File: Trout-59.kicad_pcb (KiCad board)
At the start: 2 copper layers, 304.8 x 77.8 mm, 138 parts, among them SW1 SW_Push, U1 ATmega32U4-AU, U2 SRV05-4, Y1 16MHz

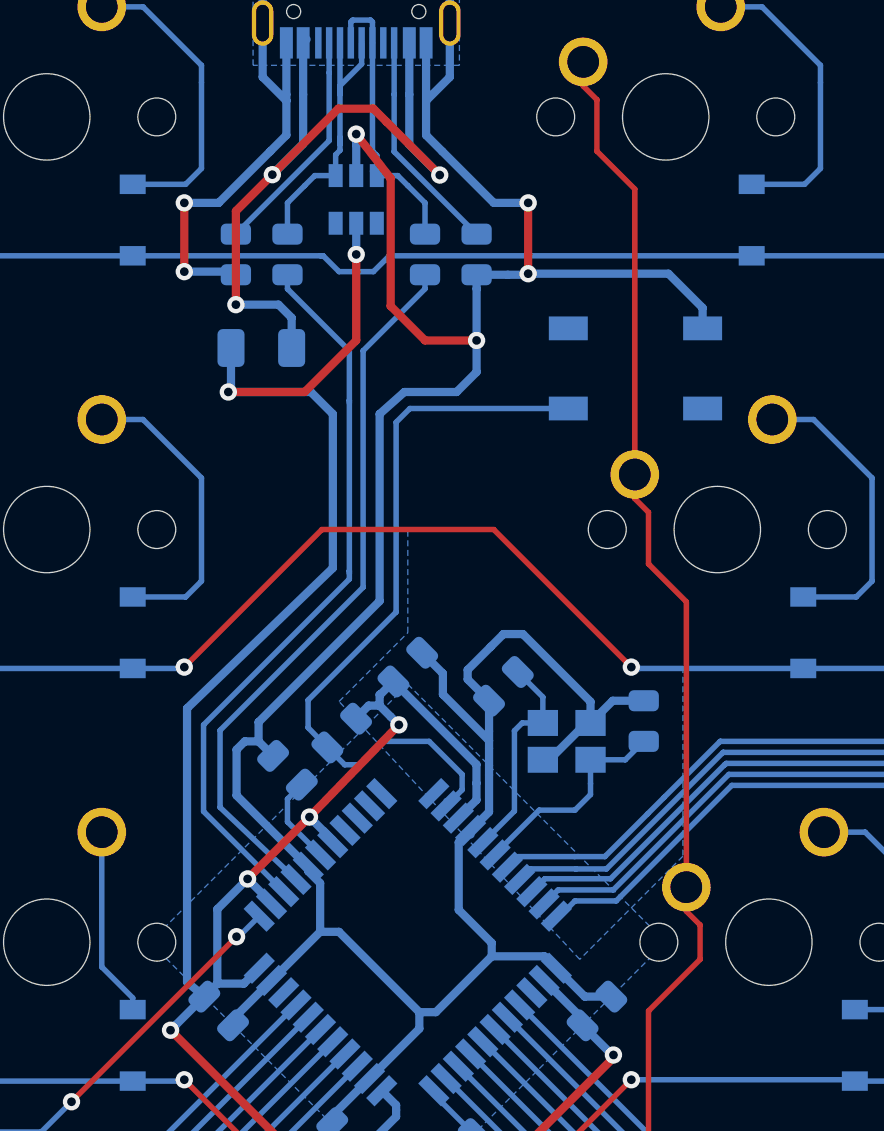
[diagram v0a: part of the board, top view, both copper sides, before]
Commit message: Multiple changes to USB/crystal routingv
Crystal ground plane defined, C2 and crystal location updated, row 0 rerouted, and Fuse rotated
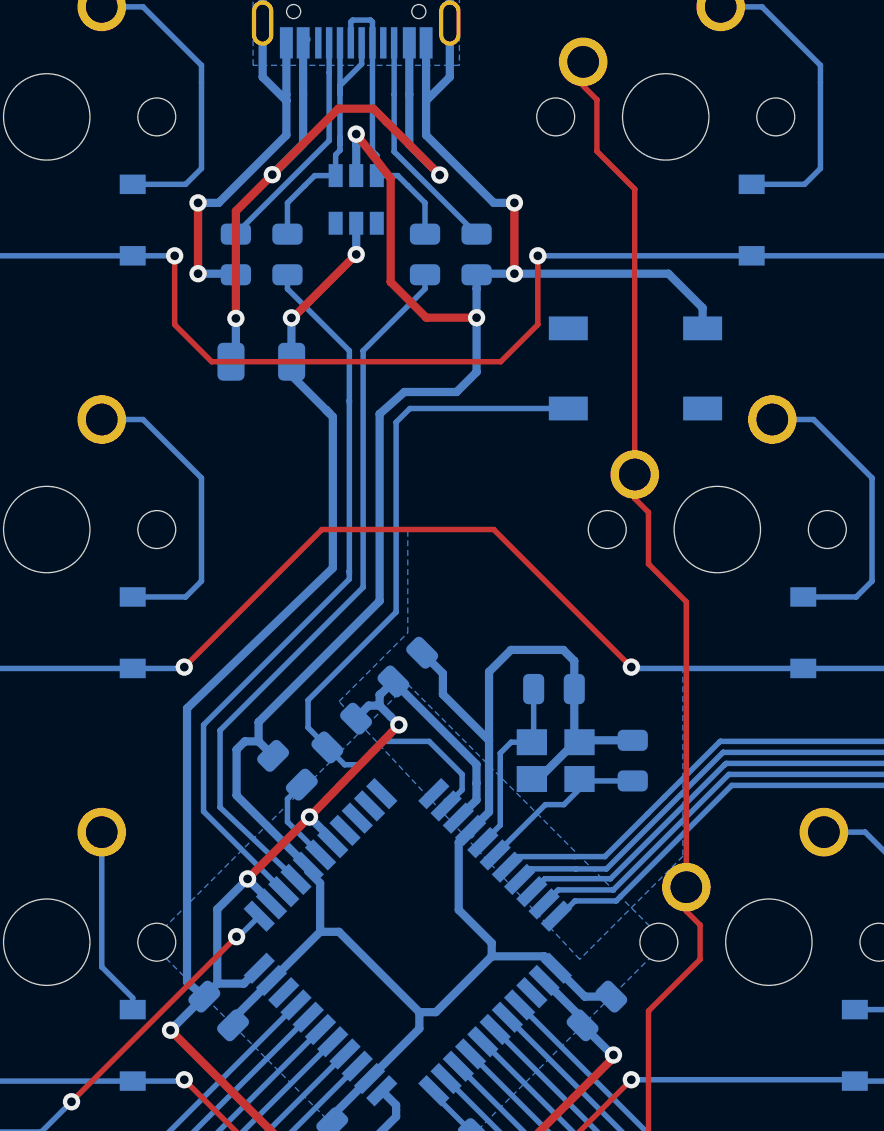
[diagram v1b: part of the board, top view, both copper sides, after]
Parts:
- moved C2 2.34 mm to (93.3, 74.0), turned to 180 degrees
- moved C1 1.90 mm to (96.9, 77.3)
- moved Y1 1.02 mm to (93.3, 77.3)
- moved F1 0.63 mm to (79.8, 58.9), turned to 180 degrees
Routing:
- net +5V: track 123.6 -> 115.0 mm
- net Row0: track 389.2 -> 396.3 mm, vias 0 -> 2
- net GND: track 195.4 -> 191.4 mm
- net VCC: track 34.8 -> 33.1 mm
- net Net-(C1-Pad2): track 10.1 -> 8.65 mm
- net Net-(C2-Pad2): track 10.1 -> 8.62 mm
